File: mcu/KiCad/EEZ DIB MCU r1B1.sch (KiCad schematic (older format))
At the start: 0 parts

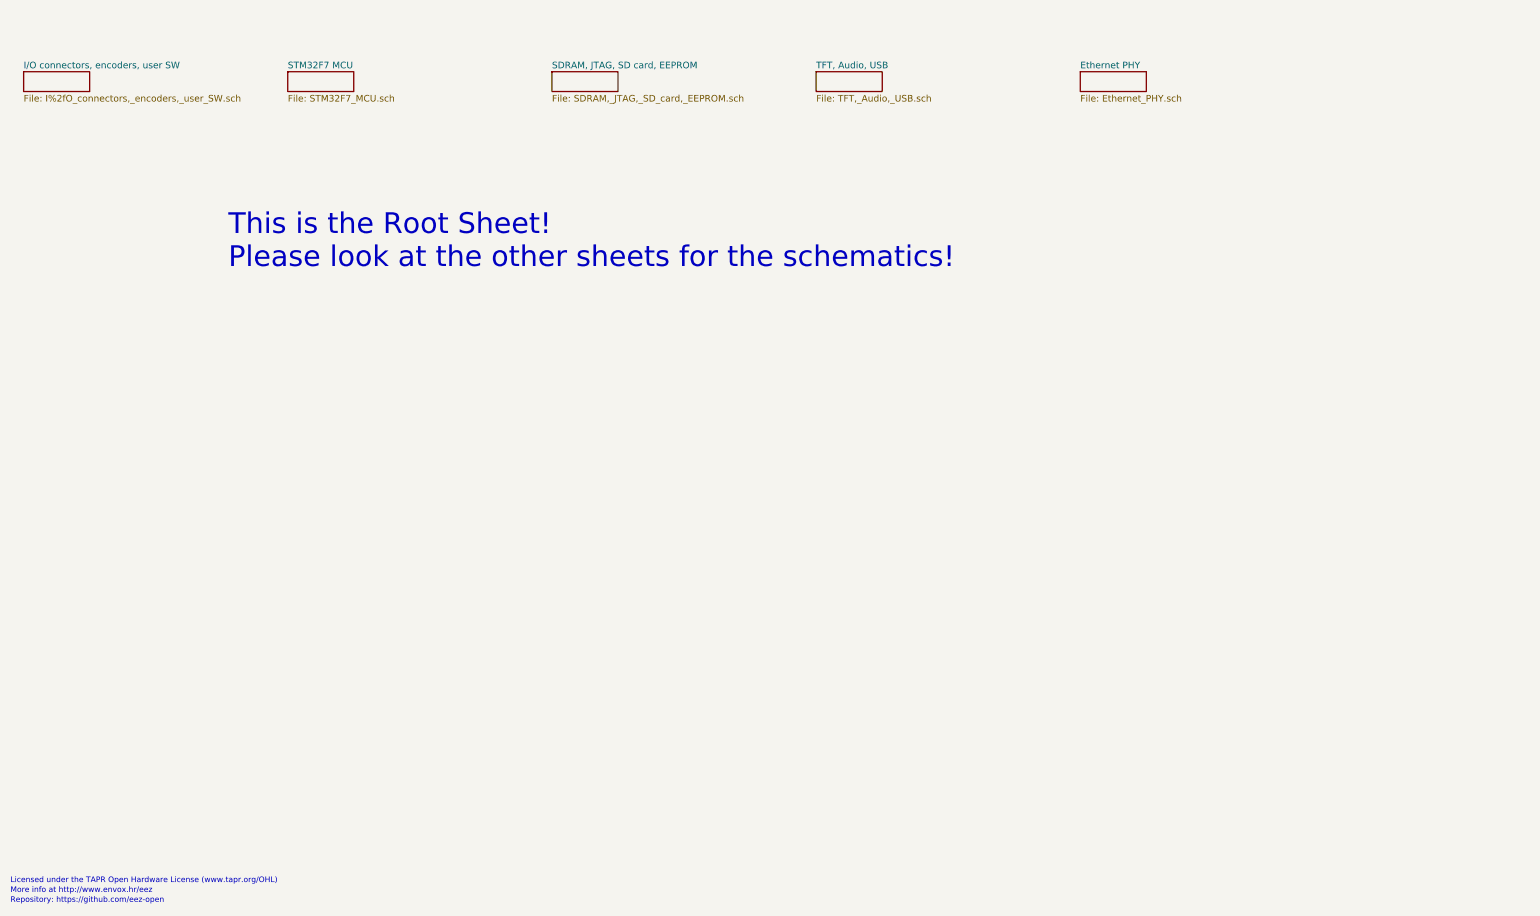
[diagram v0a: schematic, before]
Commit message: Kicad-ised schematic, fixed import errors
Basic stuff like pin functions not assigned, and moving to heirarchial labels instead of global,
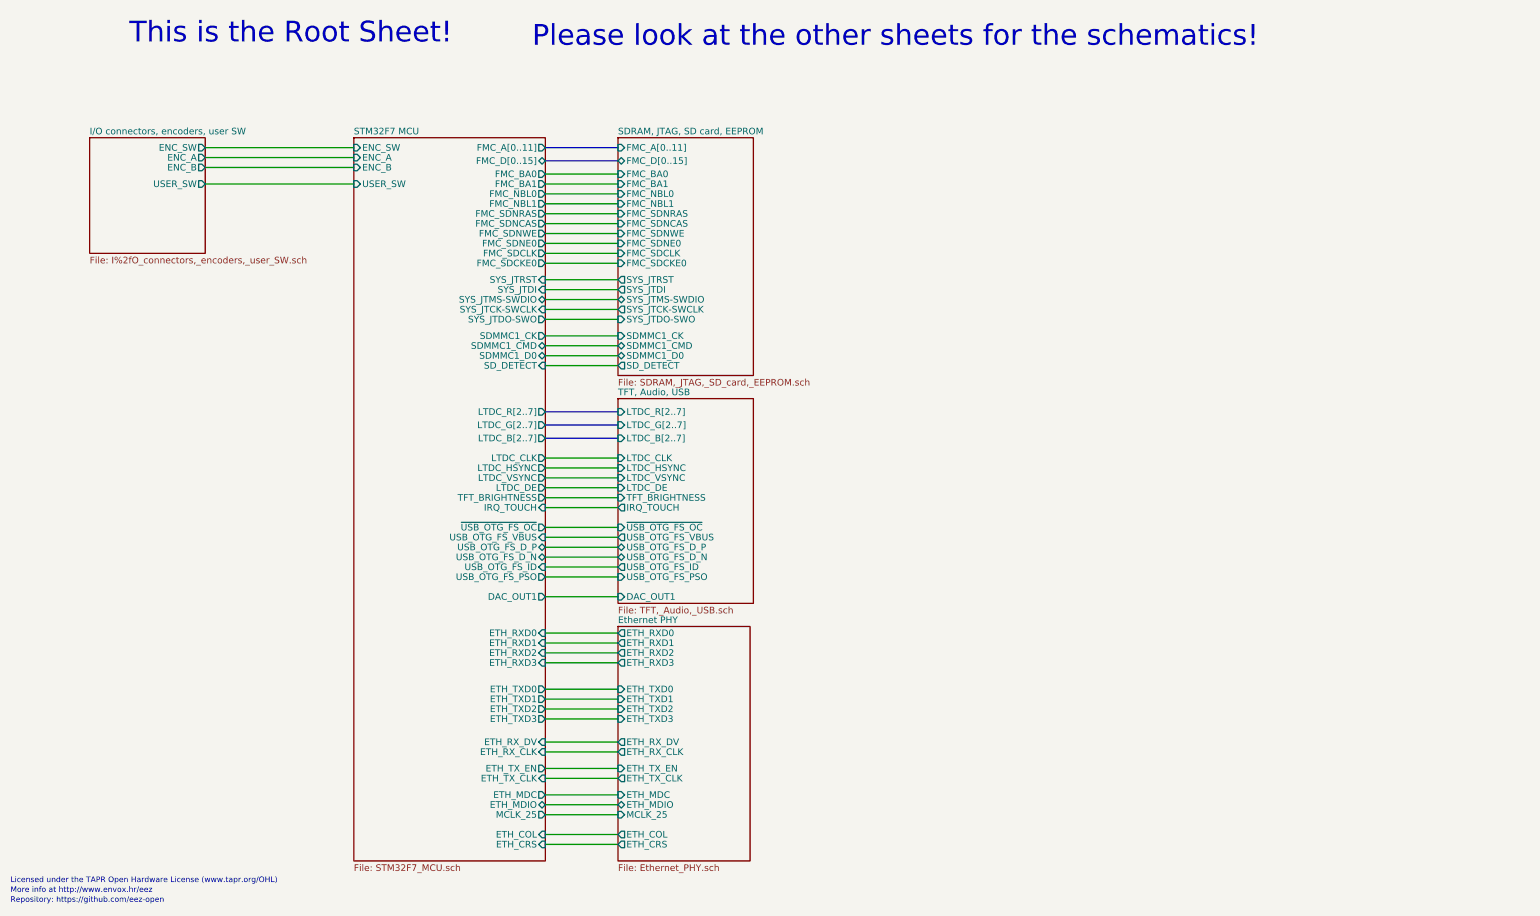
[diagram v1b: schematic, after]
